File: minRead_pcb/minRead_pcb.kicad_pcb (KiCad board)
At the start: 2 copper layers, 64 x 117 mm, 92 parts, among them J1 USB_C_Receptacle, J3 Conn_01x24, J5 Conn_01x02, J7 Micro_SD_Card, Q3 IRLML6402, Q4 Si1308EDL, Q5 AO3401A, Q6 SS8050, SW1 SW_Push, SW12 SW_Push, SW2 SW_Push, SW3 SW_Push, SW4 SW_Push, SW5 SW_Push, SW6 SW_Push, SW7 SW_Push, U1 TPD4E004DRYR, U2 BQ24074RGT, U3 AP2112K-3.3, U4 ESP32-S3-WROOM-1, U5 TPD4E004DRYR

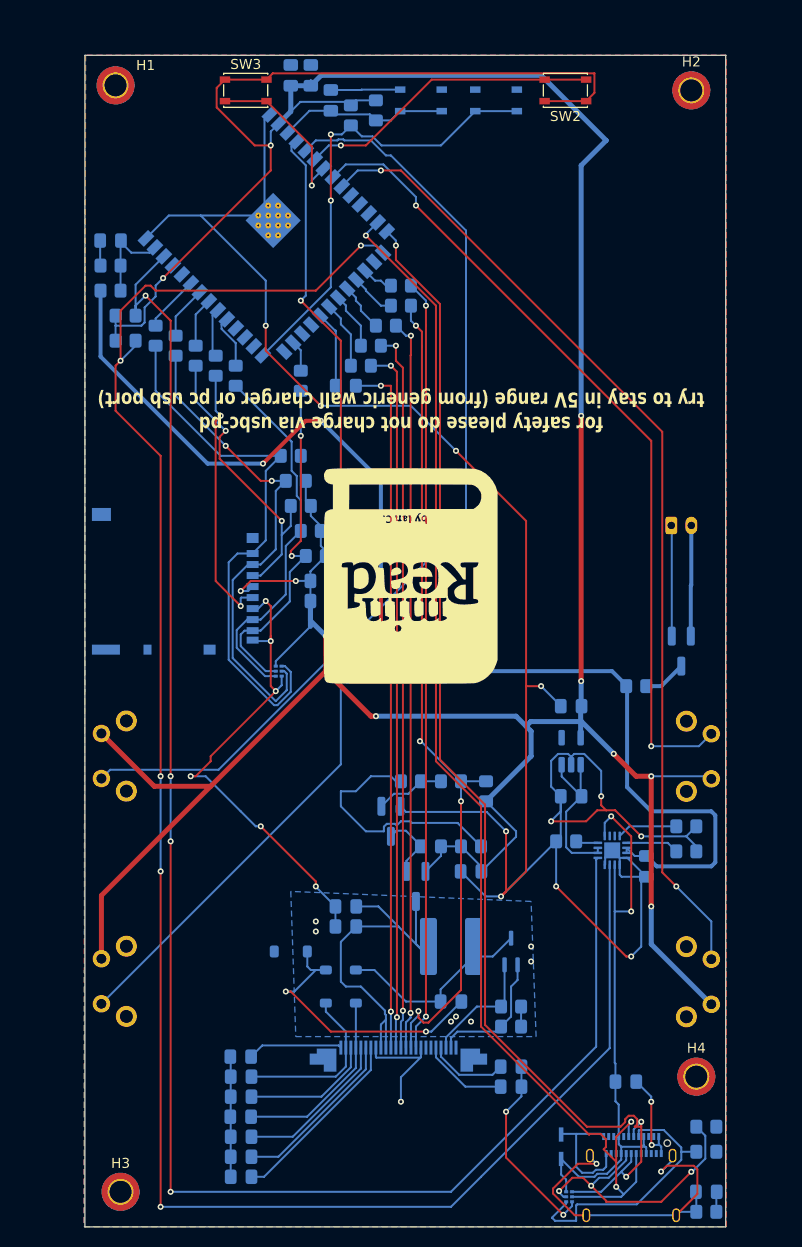
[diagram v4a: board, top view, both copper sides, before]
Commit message: gigantic commit, my bad revised schematic to sanity check turns out my fpc was flipped, now fixed added following schematics: - battery protection circuit - series LED driver - external peripheral connector for unused GPIO revised following schematics: - power path, replaced with mcp charger and FET rather than bq - buttons, opted for resistor ladder circuit, added two more for xte compatibility - eink driver, opted to change to updated components from waveshare 2.3 - updated esd components for usb-c and sdmmc - updated usb-c receptacle, now through-hole
New layout:
- mostly same as last time, but work done to ensure good grounding for LED/eink circuits
- eink gpio has minimal crossing/coupling just in case
- esp32 and 24 pin headers have longer pads hopefully for easier soldering
- external header in corner back of device
- prettier passive component layout
- fat 3v3 traces and small zone fill

- todo:
- DRC errors, mostly clearance and silkscreen overlap
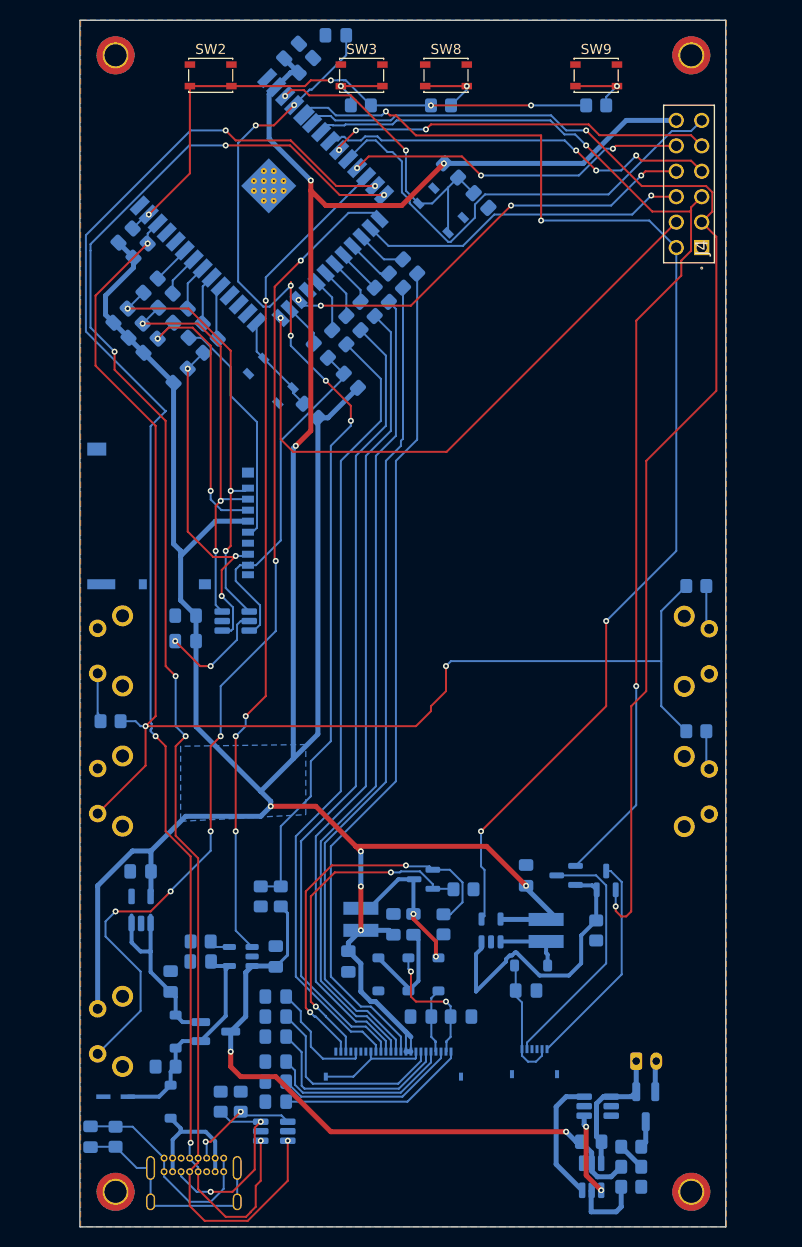
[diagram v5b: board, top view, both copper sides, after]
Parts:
- removed C21: 1u, Capacitor_SMD:C_0805_2012Metric_Pad1.18x1.45mm_HandSolder
- removed G***: LOGO, LOGO
- added C7: 0.1u, Capacitor_SMD:C_0805_2012Metric_Pad1.18x1.45mm_HandSolder, B.Cu at (158.0, 144.0)
- added C9: 1u, Capacitor_SMD:C_0805_2012Metric_Pad1.18x1.45mm_HandSolder, B.Cu at (151.5, 128.9)
- added D1: MBR0530, Diode_SMD:D_SOD-123, B.Cu at (116.0, 140.0)
- added D2: MBR0530, Diode_SMD:D_SOD-123, B.Cu at (116.5, 133.0)
- added D3: MBR0530, Diode_SMD:D_SOD-123, B.Cu at (152.0, 126.4)
- added J2: FH34SRJ-24S-0.5SH_50_, FH34SRJ-24S-0.5SH(50):HRS_FH34SRJ-24S-0.5SH_50_, B.Cu at (138.2, 136.2)
- added J4: PPTC062LFBN-RC, PPTC_12:XPYC062LFBN-RC, F.Cu at (169.0, 54.7)
- added L2: 10u, srn3010C-100m:IND_SRN3010C-100M, B.Cu at (153.5, 122.9)
- added Q1: FS8205A, Package_TO_SOT_SMD:SOT-23-6_Handsoldering, B.Cu at (158.7, 140.4)
- added Q2: IRLML6402, Package_TO_SOT_SMD:SOT-23_Handsoldering, B.Cu at (120.5, 133.0)
- added R35: 33k, Resistor_SMD:R_0805_2012Metric_Pad1.20x1.40mm_HandSolder, B.Cu at (168.5, 103.0)
- added R36: 75k, Resistor_SMD:R_0805_2012Metric_Pad1.20x1.40mm_HandSolder, B.Cu at (168.5, 88.5)
- added R37: 82, Resistor_SMD:R_0805_2012Metric_Pad1.20x1.40mm_HandSolder, B.Cu at (158.5, 122.9)
- added SW10: SW_Push, Button_Switch_THT:SW_Tactile_SPST_Angled_PTS645Vx39-2LFS, B.Cu at (108.7, 130.7)
- added SW8: SW_Push, Button_Switch_SMD:SW_SPST_PTS810, F.Cu at (143.5, 37.5)
- added SW9: SW_Push, Button_Switch_SMD:SW_SPST_PTS810, F.Cu at (158.5, 37.5)
- added U6: TPD4E1U06DBVR, Package_TO_SOT_SMD:SOT-23-6_Handsoldering, B.Cu at (126.3, 142.9)
- added U7: MCP73832-2-OT, Package_TO_SOT_SMD:SOT-23-5, B.Cu at (123.0, 125.5)
- C12: value 0.1u -> 4.7u
- H1, H2, H3, H4: moved to B.Cu
- J1: footprint Connector_USB:USB_C_Receptacle_Amphenol_12401610E4-2A -> Connector_USB:USB_C_Receptacle_GCT_USB4085
- J3: value Conn_01x24 -> FH34SRJ-6S-0.5SH_50_; footprint sfv24r:AMPHENOL_SFV24R-2STE1HLF -> FH34SRJ-6S-0.5SH(50):HRS_FH34SRJ-6S-0.5SH_50_
- L1: value 68u -> 10u; footprint Inductor_SMD:L_Changjiang_FNR6028S -> srn3010C-100m:IND_SRN3010C-100M
- Q4: value Si1308EDL -> BSS138; footprint Package_TO_SOT_SMD:SOT-323_SC-70_Handsoldering -> Package_TO_SOT_SMD:SOT-23
- Q5: value AO3401A -> BSS138; footprint Package_TO_SOT_SMD:SOT-23_Handsoldering -> Package_TO_SOT_SMD:SOT-23
- Q6: value SS8050 -> BSS138; footprint Package_TO_SOT_SMD:SOT-23_Handsoldering -> Package_TO_SOT_SMD:SOT-23
- R11: value 1.1k -> 12k
- R17: value 10k -> 100
- R18: value 47k -> 5.6k
- R19: value 47k -> 20k
- R20: value 47k -> 56k
- R28, R4: value 1.1k -> 10k
- U1: value TPD4E004DRYR -> TPD4E1U06DBVR; footprint TPD4E004DRYR:PSON50P145X100X60-6N -> Package_TO_SOT_SMD:SOT-23-6_Handsoldering
- U2: value BQ24074RGT -> AP3012; footprint Package_DFN_QFN:VQFN-16-1EP_3x3mm_P0.5mm_EP1.6x1.6mm -> Package_TO_SOT_SMD:SOT-23-5
- U5: value TPD4E004DRYR -> DW01A; footprint TPD4E004DRYR:PSON50P145X100X60-6N -> Package_TO_SOT_SMD:SOT-23-6_Handsoldering
- moved R20 75.8 mm to (158.5, 40.5)
- moved R18 74.8 mm to (135.0, 40.5), turned to 0 degrees
- moved R4 74.8 mm to (111.5, 53.5), turned to -135 degrees
- moved R19 67.6 mm to (143.0, 40.5)
- moved R10 64.8 mm to (125.0, 119.5), turned to -90 degrees
- moved R12 62.8 mm to (127.0, 119.5), turned to 90 degrees
- moved C1 61.7 mm to (108.0, 143.5), turned to -90 degrees
- moved R1 59.5 mm to (110.5, 143.5), turned to -90 degrees
- moved H2 57.6 mm to (110.5, 35.5), turned to 180 degrees
- moved H1 57.6 mm to (168.0, 35.5), turned to 180 degrees
- moved R5 57.3 mm to (115.5, 136.5), turned to 180 degrees
- moved J5 53.6 mm to (162.5, 135.9)
- moved R6 49.3 mm to (119.0, 124.0), turned to 180 degrees
- moved R2 48.8 mm to (121.0, 140.0), turned to 90 degrees
- moved R3 46.6 mm to (123.0, 140.0), turned to 90 degrees
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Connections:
- net Net-(J5-Pin_2) renamed B+
- C1 pad 1: Net-(J1-SHIELD) -> GND
- C1 pad 2: GND -> Net-(J1-SHIELD)
- C10 pad 2: /E_ink_HAT/VCC_EPD_OUT -> 3V3
- C12 pad 1: 3V3 -> GND
- C12 pad 2: GND -> 3V3
- C13 pad 2: Net-(J3-Pin_20) -> Net-(C13-Pad2)
- C14 pad 2: /E_ink_HAT/PREVGH -> /PREVGH
- C15 pad 2: Net-(J3-Pin_22) -> Net-(C15-Pad2)
- C16 pad 2: /E_ink_HAT/PREVGL -> /PREVGL
- C17 pad 2: Net-(J3-Pin_5) -> Net-(C17-Pad2)
- C18 pad 2: Net-(J3-Pin_18) -> Net-(C18-Pad2)
- C19 pad 2: Net-(J3-Pin_19) -> Net-(C19-Pad2)
- C20 pad 2: Net-(J3-Pin_24) -> Net-(C20-Pad2)
- C22 pad 2: /E_ink_HAT/VCC_EPD_OUT -> 3V3
- C3 pad 1: VBat+ -> P+
- C4 pad 1: Net-(U3-EN) -> LDO_IN
- D4 pad 2: /E_ink_HAT/PREVGL -> /PREVGL
- D5 pad 1: /E_ink_HAT/PREVGH -> /PREVGH
- J1 pad A4: USB_VBUS -> Net-(D1-A)
- J1 pad A5: /USBC_Power_Native/USBC_CC1 -> CC1
- J1 pad A6: ESP32_DP -> DP
- J1 pad A7: ESP32_DN -> DN
- J1 pad A8: unconnected-(J1-SBU1-PadA8) -> (no net)
- J1 pad A9: USB_VBUS -> Net-(D1-A)
- J1 pad B4: USB_VBUS -> Net-(D1-A)
- J1 pad B5: /USBC_Power_Native/USBC_CC2 -> CC2
- J1 pad B6: ESP32_DP -> DP
- J1 pad B7: ESP32_DN -> DN
- J1 pad B8: unconnected-(J1-SBU2-PadB8) -> (no net)
- J1 pad B9: USB_VBUS -> Net-(D1-A)
- J3 pad 1: unconnected-(J3-Pin_1-Pad1) -> LED_SW
- J3 pad 2: /E_ink_HAT/GDR -> C-
- J3 pad 3: /E_ink_HAT/RESE -> unconnected-(J3-Pad3)
- J3 pad 4: Net-(J3-Pin_4) -> unconnected-(J3-Pad4)
- J3 pad 5: Net-(J3-Pin_5) -> LED_SW
- J3 pad 6: unconnected-(J3-Pin_6-Pad6) -> W-
- J3 pad S1: (no net) -> GND
- J3 pad S2: (no net) -> GND
- J5 pad 1: GND -> B-
- J7 pad 1: Net-(J7-DAT2) -> SD_DAT2
- J7 pad 2: Net-(J7-DAT3/CD) -> SD_DAT3
- J7 pad 3: Net-(J7-CMD) -> SD_CMD
- J7 pad 5: Net-(J7-CLK) -> SD_CLK
- J7 pad 7: Net-(J7-DAT0) -> SD_DAT0
- J7 pad 8: Net-(J7-DAT1) -> SD_DAT1
- L1 pad 1: /E_ink_HAT/VCC_EPD_OUT -> Net-(D5-A)
- L1 pad 2: Net-(D5-A) -> 3V3
- Q3 pad 1: GND -> B-
- Q4 pad 1: /E_ink_HAT/GDR -> /GDR
- Q4 pad 2: /E_ink_HAT/RESE -> /RESE
- Q5 pad 1: Net-(Q5-G) -> COOL_TOGGLE
- Q5 pad 2: 3V3 -> Net-(Q5-S)
- Q5 pad 3: /E_ink_HAT/VCC_EPD_OUT -> C-
- Q6 pad 1: Net-(Q6-B) -> WARM_TOGGLE
- Q6 pad 2: GND -> Net-(Q5-S)
- Q6 pad 3: Net-(Q5-G) -> W-
- R11 pad 1: CHG_STATUS -> Net-(R11-Pad1)
- R11 pad 2: 3V3 -> BUTTON_ADC_2
- R12 pad 1: VBat+ -> P+
- R14 pad 2: /E_ink_HAT/RESE -> /RESE
- R15 pad 2: /E_ink_HAT/GDR -> /GDR
- R16 pad 1: EPD_RST -> GND
- R16 pad 2: 3V3 -> Net-(U5-CS)
- R17 pad 1: Net-(Q6-B) -> P+
- R17 pad 2: EPD_RST -> Net-(R17-Pad2)
- R18 pad 2: 3V3 -> BUTTON_ADC_1
- R19 pad 1: Net-(Q6-B) -> Net-(R19-Pad1)
- R19 pad 2: Net-(R18-Pad1) -> BUTTON_ADC_1
- R2 pad 1: /USBC_Power_Native/USBC_CC1 -> CC2
- R20 pad 1: 3V3 -> Net-(R20-Pad1)
- R20 pad 2: Net-(Q5-G) -> BUTTON_ADC_1
- R21 pad 1: SD_DAT0 -> Net-(U4-IO42)
- R21 pad 2: Net-(J7-DAT0) -> SD_DAT2
- R22 pad 1: SD_DAT1 -> Net-(U4-IO41)
- R22 pad 2: Net-(J7-DAT1) -> SD_DAT3
- R23 pad 1: SD_DAT2 -> Net-(U4-IO40)
- R23 pad 2: Net-(J7-DAT2) -> SD_CMD
- R24 pad 1: SD_DAT3 -> Net-(U4-IO38)
- R24 pad 2: Net-(J7-DAT3/CD) -> SD_DAT0
- R25 pad 1: SD_CLK -> Net-(U4-IO39)
- R25 pad 2: Net-(J7-CLK) -> SD_CLK
- R26 pad 1: SD_CMD -> Net-(U4-IO48)
- R26 pad 2: Net-(J7-CMD) -> SD_DAT1
- R27 pad 1: VBat+ -> Net-(R17-Pad2)
- R28 pad 1: PGOOD -> BUTTON_ADC_2
- R29 pad 1: EPD_BUSY -> EPD_MOSI
- R3 pad 1: /USBC_Power_Native/USBC_CC2 -> CC1
- R30 pad 1: EPD_RST -> EPD_SCK
- R31 pad 1: EPD_DC -> EPD_CS
- R32 pad 1: EPD_CS -> EPD_DC
- R33 pad 1: EPD_SCK -> EPD_RST
- R34 pad 1: EPD_MOSI -> EPD_BUSY
- R4 pad 1: Net-(U2-ILIM) -> BUTTON_ADC_1
- R4 pad 2: GND -> 3V3
- R5 pad 1: Net-(U2-ISET) -> USB_VBUS
- R53 pad 1: Net-(J7-DAT2) -> SD_DAT2
- R54 pad 1: Net-(J7-DAT3/CD) -> SD_DAT3
- R55 pad 1: Net-(J7-CMD) -> SD_CMD
- R6 pad 1: Net-(U2-TS) -> Net-(U7-PROG)
- R8 pad 1: Net-(J7-DAT0) -> SD_DAT0
- R9 pad 1: Net-(J7-DAT1) -> SD_DAT1
- SW1 pad 1: 3V3 -> GND
- SW1 pad 2: DPAD_UP -> BUTTON_ADC_2
- SW2 pad 1: 3V3 -> GND
- SW2 pad 2: DPAD_LEFT -> BUTTON_ADC_1
- SW3 pad 1: 3V3 -> GND
- SW3 pad 2: DPAD_RIGHT -> Net-(R18-Pad1)
- SW4 pad 1: 3V3 -> GND
- SW4 pad 2: DPAD_DOWN -> Net-(R11-Pad1)
- SW5 pad 1: 3V3 -> GND
- SW5 pad 2: BUTTON_A -> Net-(R35-Pad1)
- SW7 pad 1: 3V3 -> GND
- SW7 pad 2: BUTTON_B -> Net-(R36-Pad1)
- U1 pad 1: Net-(J7-DAT2) -> SD_DAT2
- U1 pad 2: Net-(J7-DAT3/CD) -> GND
- U1 pad 3: GND -> SD_DAT1
- U1 pad 4: Net-(J7-DAT0) -> SD_DAT0
- U1 pad 5: Net-(J7-DAT1) -> (no net)
- U1 pad 6: 3V3 -> SD_DAT3
- U2 pad 1: Net-(U2-TS) -> Net-(D3-A)
- U2 pad 2: VBat+ -> GND
- U2 pad 3: VBat+ -> Net-(Q5-S)
- U2 pad 4: GND -> PWM_LED
- U2 pad 5: GND -> 3V3
- U3 pad 1: Net-(U3-EN) -> LDO_IN
- U3 pad 3: Net-(U3-EN) -> LDO_IN
- U4 pad 10: unconnected-(U4-IO17-Pad10) -> UNUSED_GPIO_17
- U4 pad 11: unconnected-(U4-IO18-Pad11) -> UNUSED_GPIO_18
- U4 pad 12: unconnected-(U4-IO8-Pad12) -> CHG_STATUS
- U4 pad 13: ESP32_DN -> DN
- U4 pad 14: ESP32_DP -> DP
- U4 pad 15: PGOOD -> PWR_BUTTON
- U4 pad 16: unconnected-(U4-IO46-Pad16) -> UNUSED_GPIO_46
- U4 pad 24: unconnected-(U4-IO47-Pad24) -> UNUSED_GPIO_47
- U4 pad 25: SD_DAT1 -> Net-(U4-IO48)
- U4 pad 26: unconnected-(U4-IO45-Pad26) -> UNUSED_GPIO_45
- U4 pad 31: SD_DAT0 -> Net-(U4-IO38)
- U4 pad 32: SD_CLK -> Net-(U4-IO39)
- U4 pad 33: SD_CMD -> Net-(U4-IO40)
- U4 pad 34: SD_DAT3 -> Net-(U4-IO41)
- U4 pad 35: SD_DAT2 -> Net-(U4-IO42)
- U4 pad 38: CHG_STATUS -> BUTTON_ADC_2
- U4 pad 39: BAT_MONIT -> BUTTON_ADC_1
- U4 pad 4: DPAD_UP -> BAT_MONIT
- U4 pad 5: DPAD_DOWN -> PWM_LED
- U4 pad 6: DPAD_LEFT -> WARM_TOGGLE
- U4 pad 7: DPAD_RIGHT -> COOL_TOGGLE
- U4 pad 8: BUTTON_B -> UNUSED_GPIO_15
- U4 pad 9: BUTTON_A -> UNUSED_GPIO_16
- U5 pad 1: ESP32_DP -> Net-(U5-OD)
- U5 pad 2: ESP32_DN -> Net-(U5-CS)
- U5 pad 3: GND -> Net-(U5-OC)
- U5 pad 4: /USBC_Power_Native/USBC_CC1 -> unconnected-(U5-TD-Pad4)
- U5 pad 5: /USBC_Power_Native/USBC_CC2 -> P+
- U5 pad 6: USB_VBUS -> B-
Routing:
- net GND: track 361.2 -> 43.4 mm, vias 29 -> 2
- net PGOOD: track 193.5 -> 0.00 mm, vias 5 -> 0
- net DP: track 0.00 -> 153.6 mm, vias 0 -> 6
- net DN: track 0.00 -> 151.0 mm, vias 0 -> 5
- net BUTTON_ADC_2: track 0.00 -> 141.6 mm, vias 0 -> 3
- net ESP32_DN: track 125.2 -> 0.00 mm, vias 3 -> 0
- net WARM_TOGGLE: track 0.00 -> 124.3 mm, vias 0 -> 2
- net PWM_LED: track 0.00 -> 124.0 mm, vias 0 -> 4
- net VBat+: track 122.2 -> 0.00 mm, vias 4 -> 0
- net ESP32_DP: track 121.6 -> 0.00 mm, vias 3 -> 0
- net COOL_TOGGLE: track 0.00 -> 113.3 mm, vias 0 -> 2
- net PWR_BUTTON: track 0.00 -> 102.9 mm, vias 0 -> 6
- net DPAD_UP: track 98.7 -> 0.00 mm, vias 2 -> 0
- net BUTTON_A: track 98.2 -> 0.00 mm, vias 2 -> 0
- net DPAD_DOWN: track 96.4 -> 0.00 mm
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- added copper zone on B.Cu, net 3V3
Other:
- board size 64 x 117 mm -> 64.5 x 120.5 mm
- board text removed: "BOOT"
- board text removed: "RST"
- board text removed: "for safety please do not charge via usbc-pd try to stay in 5V range (from generic wall charger or pc usb port)"
- board text removed: "place 24-pin eink header here pls"
- board text removed: "place esp32-s3 here pls"
- board text removed: "place sd card here pls"

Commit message: updated some things: - confirmed battery protection circuit - added pull up to EPD_RST - changed to 10 pin external IO header instead of 12 pin - reserved gpio 17 and 18 for LED_PWR and LED_SENSE - responsible for providing 3.3V to LED circuit and detecting if the circuit is closed or not (for safety) - these are pulled high with 10k so that the LED circuit does not start unless told to in software, and that LED_SENSE goes low when it detects current through LEDs (kind of, not really, but same principle) - added indicator for inductor name - made pull down on vbus stronger for less current draw while plugged in - changed battery monitor resistors to 1M/1M for less current draw, period - added some comments on schematic - layout is done, just has a couple of minor silkscreen warnings - basically all keep-outs are gone, btw. we like to live dangerously - I think that's it?
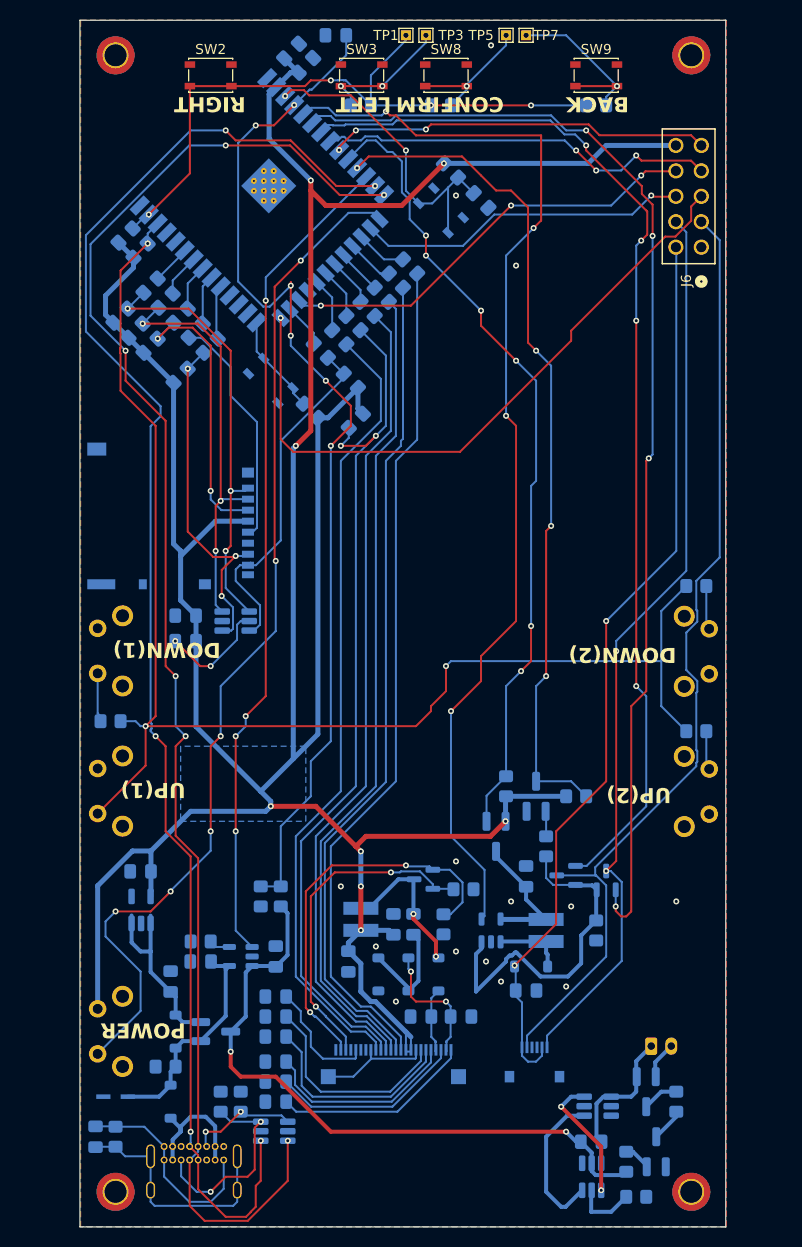
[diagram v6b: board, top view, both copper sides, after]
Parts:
- removed D3: MBR0530, Diode_SMD:D_SOD-123
- removed J4: PPTC062LFBN-RC, PPTC_12:XPYC062LFBN-RC
- added D7: MBR0540, Diode_SMD:D_SOD-123, B.Cu at (152.0, 126.5)
- added J6: PPTC052LFBN-RC, PPTC_10:CONN_PPTC052LFBN-RC_SUL, F.Cu at (169.0, 54.7)
- added Q7: IRLML6402, Package_TO_SOT_SMD:SOT-23_Handsoldering, B.Cu at (148.5, 113.5)
- added Q8: IRLML6402, Package_TO_SOT_SMD:SOT-23_Handsoldering, B.Cu at (164.5, 145.0)
- added Q9: MMBT3904, Package_TO_SOT_SMD:SOT-23_Handsoldering, B.Cu at (152.5, 109.5)
- added R38: 100k, Resistor_SMD:R_0805_2012Metric_Pad1.20x1.40mm_HandSolder, B.Cu at (115.5, 136.5)
- added R39: 10k, Resistor_SMD:R_0805_2012Metric_Pad1.20x1.40mm_HandSolder, B.Cu at (153.5, 114.5)
- added R40: 10k, Resistor_SMD:R_0805_2012Metric_Pad1.20x1.40mm_HandSolder, B.Cu at (149.5, 108.5)
- added R41: 10k, Resistor_SMD:R_0805_2012Metric_Pad1.20x1.40mm_HandSolder, B.Cu at (156.5, 109.5)
- added TP1: TestPoint, TestPoint:TestPoint_THTPad_1.0x1.0mm_Drill0.5mm, F.Cu at (139.5, 33.5)
- added TP3: TestPoint, TestPoint:TestPoint_THTPad_1.0x1.0mm_Drill0.5mm, F.Cu at (141.5, 33.5)
- added TP5: TestPoint, TestPoint:TestPoint_THTPad_1.0x1.0mm_Drill0.5mm, F.Cu at (149.5, 33.5)
- added TP7: TestPoint, TestPoint:TestPoint_THTPad_1.0x1.0mm_Drill0.5mm, F.Cu at (151.5, 33.5)
- R10: value 47k -> 1M
- R12: value 100k -> 1M
- R36: value 75k -> 68k
- R5: value 8.9k -> 10k
- moved R5 67.2 mm to (134.5, 72.0), turned to 45 degrees
- moved R27 6.36 mm to (166.5, 140.0), turned to 90 degrees
- moved J5 2.12 mm to (164.0, 134.4)
- moved Q3 1.50 mm to (163.5, 139.0)
- moved J1 1.16 mm to (121.3, 144.5)
- moved R16 1.12 mm to (162.5, 149.5)
- moved R17 0.71 mm to (161.5, 146.0), turned to 90 degrees
- moved C1 0.50 mm to (108.5, 143.5)
- moved C12 0.10 mm to (151.5, 117.5)
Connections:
- net Net-(R18-Pad1) renamed LEFT
- net Net-(R19-Pad1) renamed CONFIRM
- net Net-(R20-Pad1) renamed BACK
- C12 pad 2: 3V3 -> Net-(Q7-D)
- L2 pad 1: 3V3 -> Net-(Q7-D)
- Q1 pad 4: Net-(U5-OD) -> Net-(U5-OC)
- Q1 pad 6: Net-(U5-OC) -> Net-(U5-OD)
- R17 pad 2: Net-(R17-Pad2) -> Net-(Q8-S)
- R27 pad 1: Net-(R17-Pad2) -> Net-(Q8-D)
- R5 pad 1: USB_VBUS -> EPD_RST
- R5 pad 2: GND -> 3V3
- U2 pad 5: 3V3 -> Net-(Q7-D)
- U4 pad 10: UNUSED_GPIO_17 -> LED_PWR
- U4 pad 11: UNUSED_GPIO_18 -> LED_SENSE
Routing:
- net LED_SENSE: track 0.00 -> 84.2 mm, vias 0 -> 4
- net LED_PWR: track 0.00 -> 80.5 mm, vias 0 -> 6
- net LED_SW: track 12.5 -> 90.8 mm, vias 0 -> 2
- net C-: track 25.0 -> 97.0 mm
- net W-: track 21.8 -> 90.2 mm, vias 0 -> 2
- net UNUSED_GPIO_17: track 48.1 -> 0.00 mm
- net UNUSED_GPIO_18: track 34.4 -> 0.00 mm, vias 3 -> 0
- net Net-(Q7-D): track 0.00 -> 14.6 mm
- net PWM_LED: track 124.0 -> 109.8 mm
- net BACK: track 6.52 -> 17.7 mm
- net WARM_TOGGLE: track 124.3 -> 114.4 mm, vias 2 -> 4
- net BUTTON_ADC_1: track 57.6 -> 66.0 mm
- net LEFT: track 6.49 -> 13.4 mm, vias 1 -> 2
- net CONFIRM: track 6.73 -> 13.4 mm
- net COOL_TOGGLE: track 113.3 -> 106.9 mm, vias 2 -> 4
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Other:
- board text added: "BACK"
- board text added: "CONFIRM"
- board text added: "DOWN(1)"
- board text added: "DOWN(2)"
- board text added: "LEFT"
- board text added: "POWER"
- board text added: "RIGHT"
- board text added: "UP(1)"
- board text added: "UP(2)"
